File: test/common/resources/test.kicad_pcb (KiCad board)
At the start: 2 copper layers, 3 parts

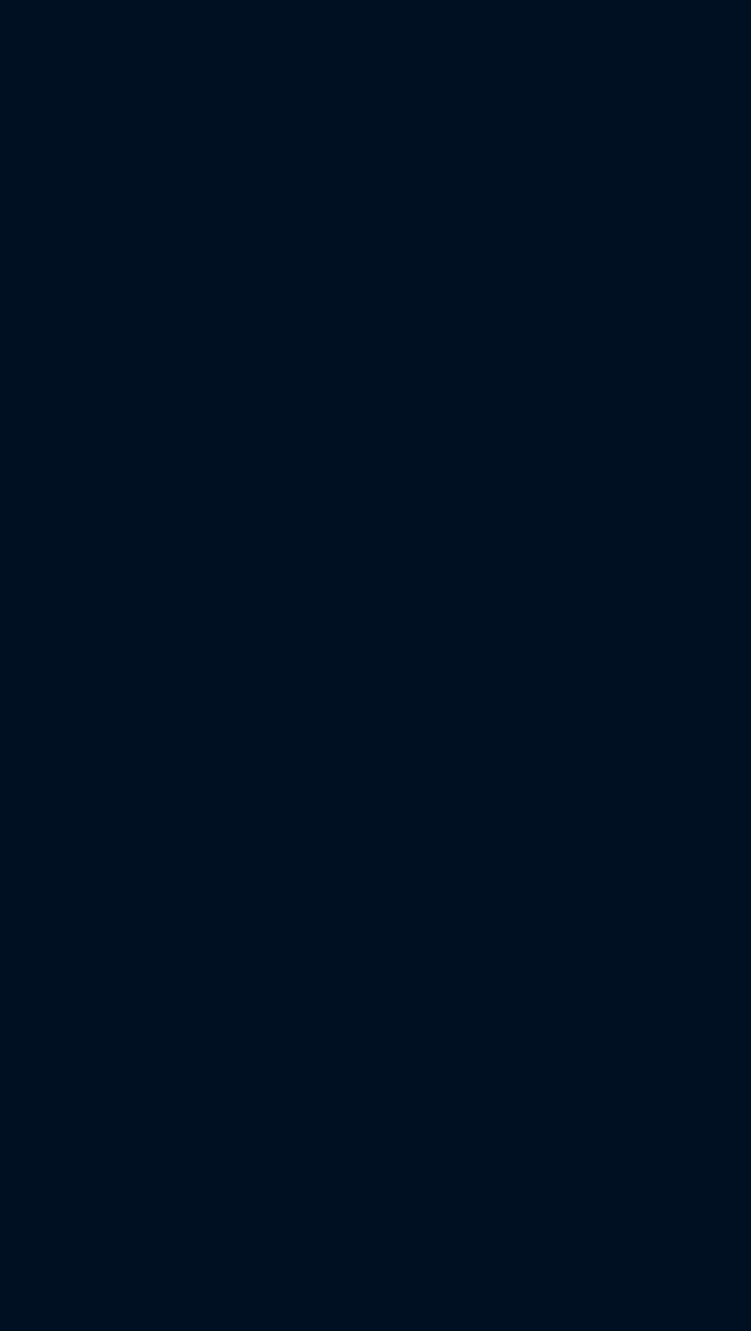
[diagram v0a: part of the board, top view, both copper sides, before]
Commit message: Libs: KiCad: Extend fileformat (#243)
* Add support for layerstackup

* Various additions and small fixes in fileformat

* Fix: default values for zones

* Fix: Add order & fix enums & add test cases

* Fix: support multiple pads in trait has_linked_kicad_pad_defined

* Fix: layers in insert_zone

* Fix: Assert for multiple same pads in footprint

---------

Co-authored-by: iopapamanoglou <ioannis@atopile.io>
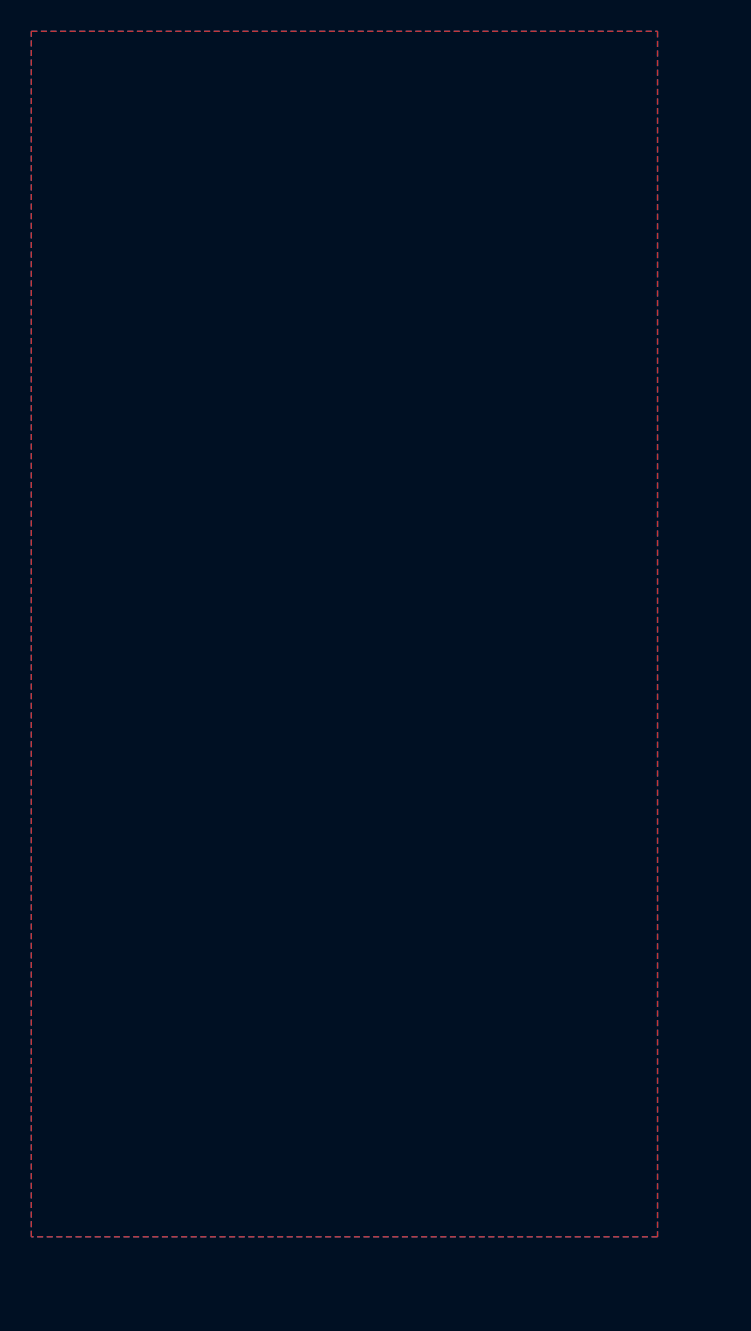
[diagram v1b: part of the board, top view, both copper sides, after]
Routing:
- added copper zone on B.Cu, net GND
- added copper zone on F.Cu, net GND
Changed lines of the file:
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@@
         (58 "User.9" user))
     (setup
+        (stackup
+            (layer "F.SilkS"
+                (type "Top Silk Screen") )
+            (layer "F.Paste"
+                (type "Top Solder Paste") )
+            (layer "F.Mask"
+                (type "Top Solder Mask")
+                (color "Green")
+                (thickness 0.01524)
+                (material "Epoxy")
+                (epsilon_r 3.8)
+                (loss_tangent 0) )
+            (layer "F.Cu"
+                (type "copper")
+                (thickness 0.035) )
+            (layer "dielectric 1"
+                (type "prepreg")
+                (color "FR4 natural")
+                (thickness 0.0994)
+                (material "FR4")
+                (epsilon_r 4.1)
+                (loss_tangent 0.02) )
+            (layer "In1.Cu"
+                (type "copper")
+                (thickness 0.0152) )
+            (layer "dielectric 2"
+                (type "core")
+                (color "FR4 natural")
+                (thickness 1.24)
+                (material "FR4")
+                (epsilon_r 4.43)
+                (loss_tangent 0.02) )
+            (layer "In2.Cu"
+                (type "copper")
+                (thickness 0.0152) )
+            (layer "dielectric 3"
+                (type "prepreg")
+                (color "FR4 natural")
+                (thickness 0.0994)
+                (material "FR4")
+                (epsilon_r 4.1)
+                (loss_tangent 0.02) )
+            (layer "B.Cu"
+                (type "copper")
+                (thickness 0.035) )
+            (layer "B.Mask"
+                (type "Bottom Solder Mask")
+                (color "Green")
+                (thickness 0.01524)
+                (material "Epoxy")
+                (epsilon_r 3.8)
+                (loss_tangent 0) )
+            (layer "B.Paste"
+                (type "Bottom Solder Paste") )
+            (layer "B.SilkS"
+                (type "Bottom Silk Screen") )
+            (copper_finish "HAL SnPb")
+            (dielectric_constraints yes))
         (pad_to_mask_clearance 0)
         (allow_soldermask_bridges_in_footprints no)
@@
             (drillshape 1)
             (scaleselection 1)
-            (outputdirectory "")))
+            (outputdirectory "")) )
     (net 0 "")
     (net 1 "B1-1-R1-2")
@@
                 (xyz 1 1 1))
             (rotate
-                (xyz 0 0 0)))))
+                (xyz 0 0 0))))
+    (zone
+        (net 2)
+        (net_name "GND")
+        (layers "F.Cu" "In1.Cu" "In2.Cu" "B.Cu")
+        (name "layer_fill_GND")
+        (hatch edge 0.5)
+        (connect_pads
+            (clearance 0.2)		)
+        (min_thickness 0.2)
+        (filled_areas_thickness no)
+        (fill yes
+            (thermal_gap 0.2)
+            (thermal_bridge_width 0.2)
+            (island_removal_mode 2)
+            (island_area_min 10)		)
+        (polygon
+            (pts
+                (xy -20 -1)
+                (xy 20 -1)
+                (xy 20 76)
+                (xy -20 76)			)		)))

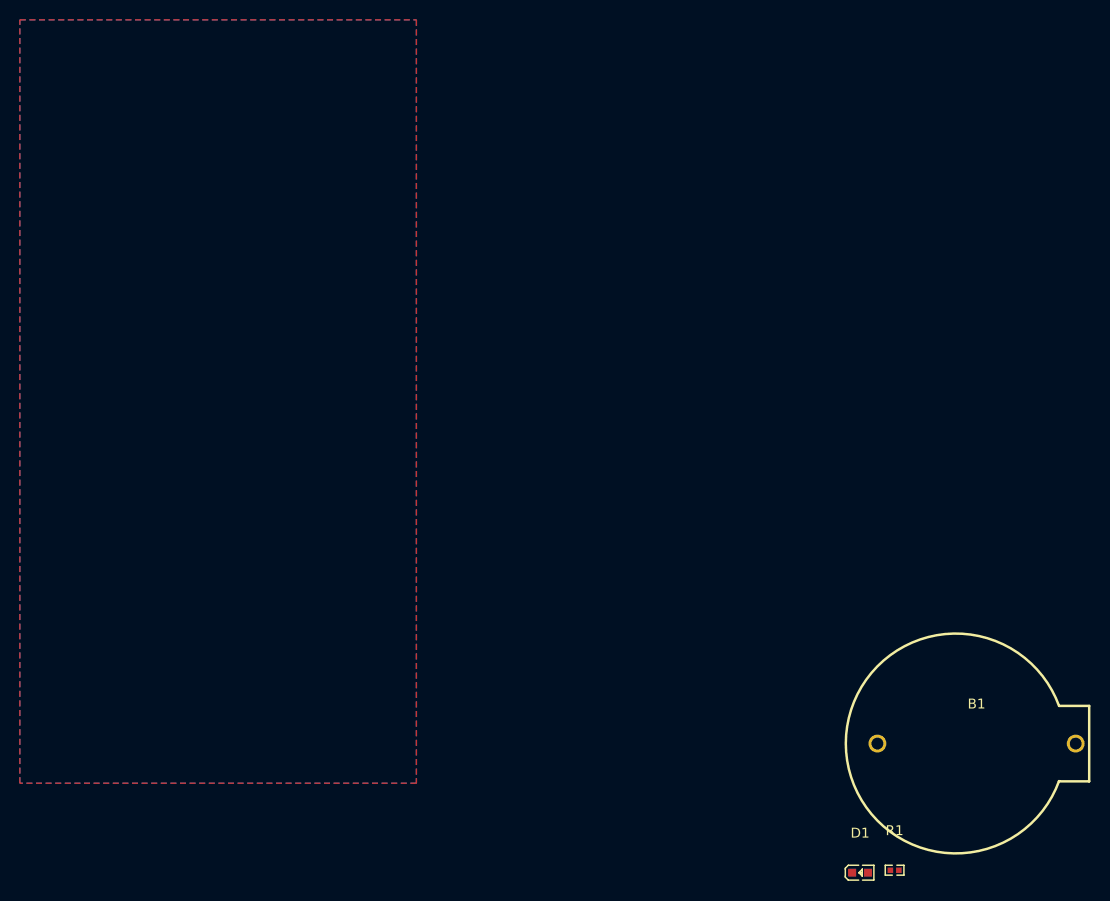
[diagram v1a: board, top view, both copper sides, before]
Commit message: Bugfix: missing kicad fileformat items (#256)
* Fix: pcb footprint pad default net

* Fix: footrpint multiple attributes

* Fix: missing:
  - footprint attr
  - footprint pad type
  - filled zone pour
  - support for keepout zone
  - support for sheets info in kicad project file

* Add: keepout zone to test pcb file

* Fix: zone fill enable default

* Add: filled zones to zone

* Add: allow_missing_courtyard to fileformat (#259)

* Give multidict default values; Fix filled polygon

---------

Co-authored-by: Matt Wildoer <mawildoer@gmail.com>
Co-authored-by: iopapamanoglou <ioannis@atopile.io>
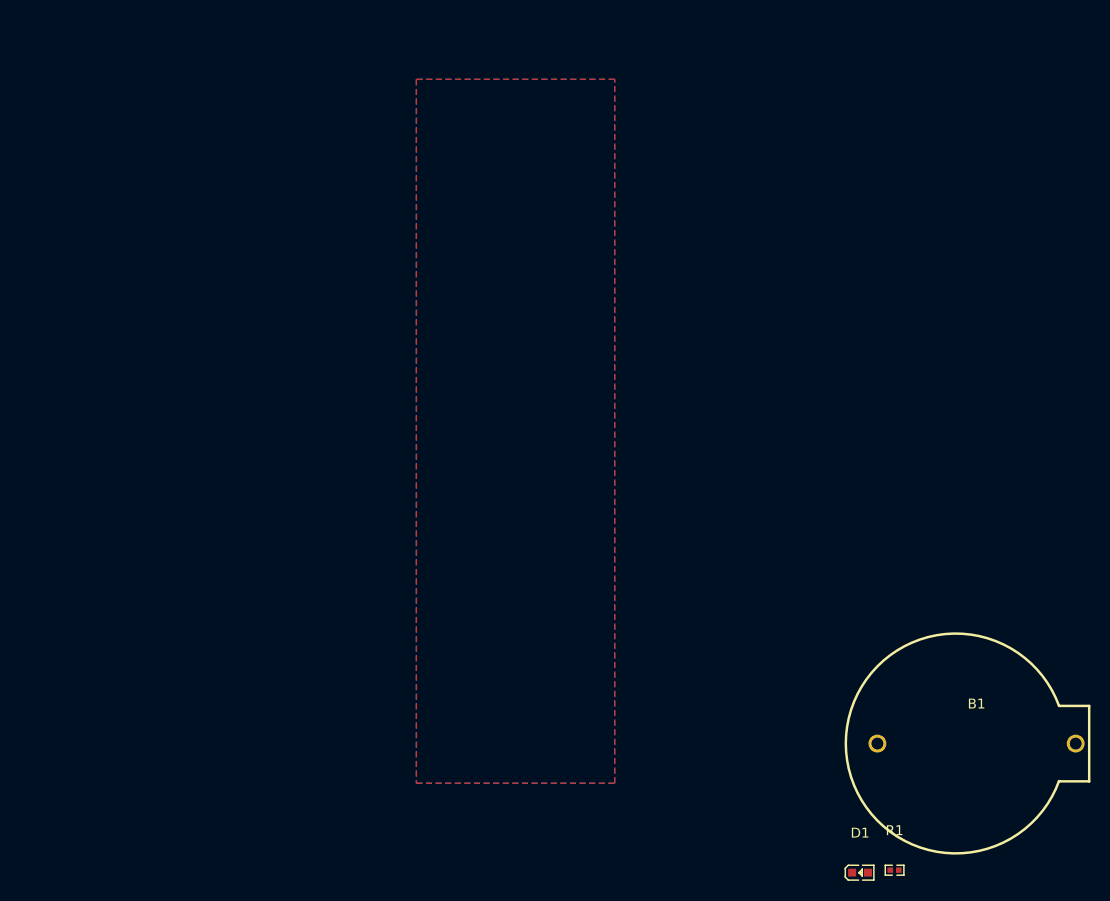
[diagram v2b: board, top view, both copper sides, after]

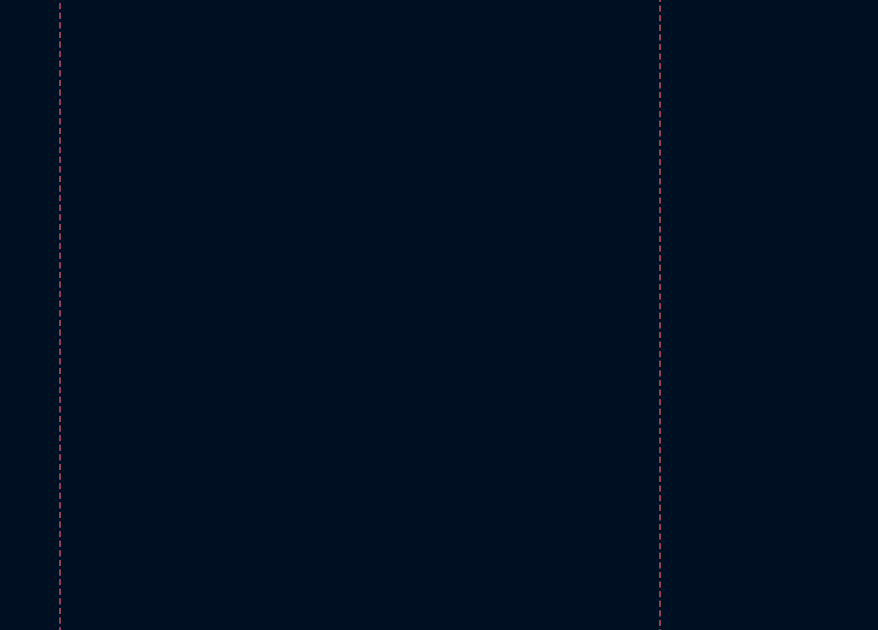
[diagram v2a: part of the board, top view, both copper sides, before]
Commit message: Bugfix: kicad: fileformats: add missing items (#24)
* Add: generic fill enum

* Add: missing footprint polygons

* Add: support mulitple 3d files in footprint

* Fix: spelling

* Add: faebryk logo to test pcb file

* Add: faebryk logo fp
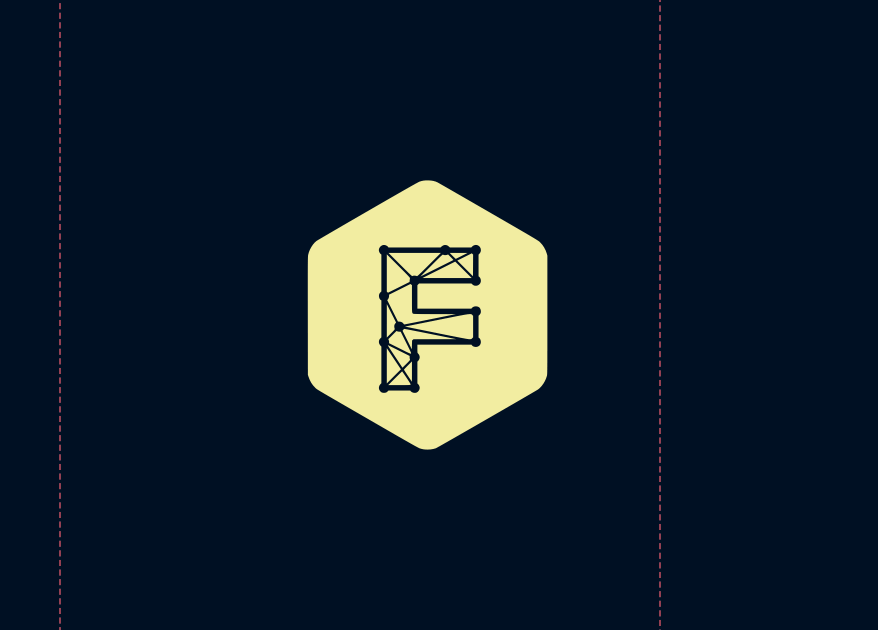
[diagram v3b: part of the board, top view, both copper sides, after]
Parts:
- added G***: LOGO, logos:faebryk_logo, F.Cu at (32.2, 46.8)
